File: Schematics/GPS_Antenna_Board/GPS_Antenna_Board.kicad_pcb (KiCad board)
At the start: 2 copper layers, 50 x 65 mm, 22 parts, among them J2 470804001, U1 SAM-M10Q, U2 LM66100DCKR

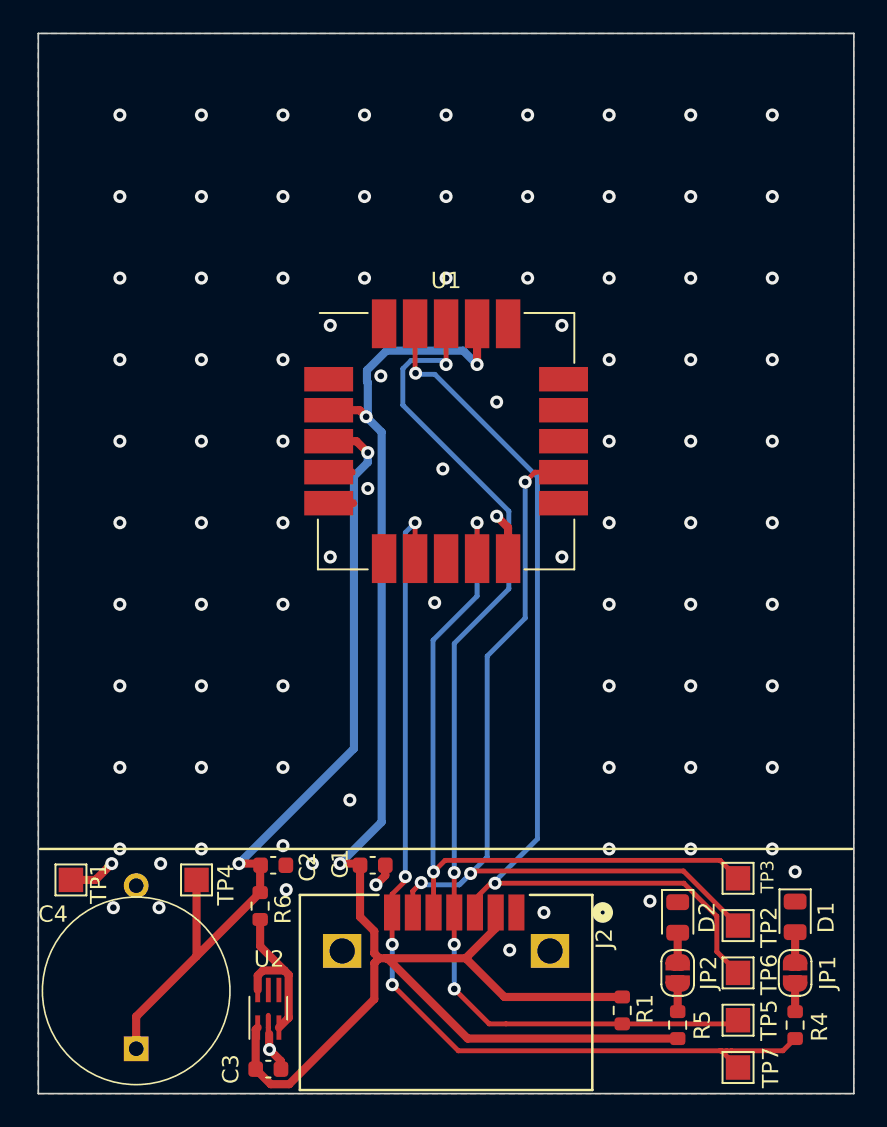
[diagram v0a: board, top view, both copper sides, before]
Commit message: Added mounting holes to GPS antenna board
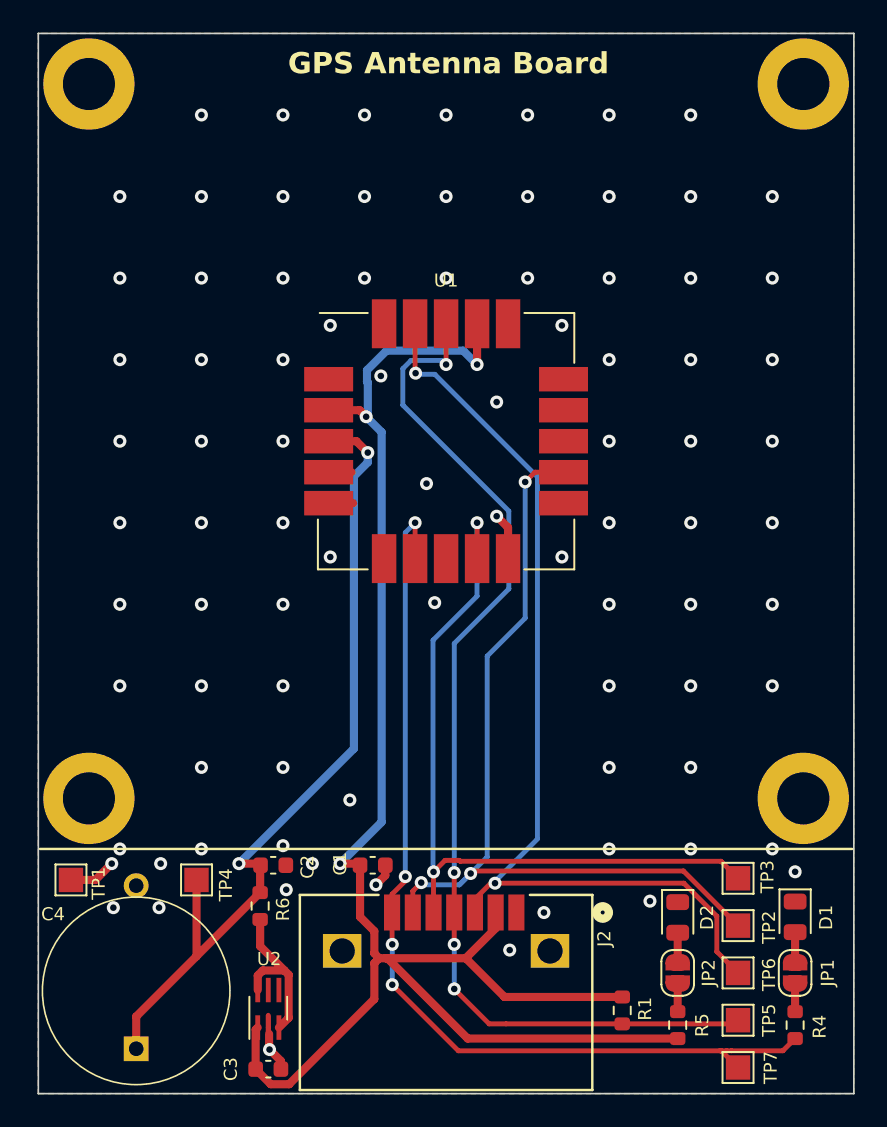
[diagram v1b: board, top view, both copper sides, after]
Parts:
- added H1: MountingHole, MountingHole:MountingHole_3.2mm_M3_DIN965_Pad, F.Cu at (125.8, 77.3)
- added H2: MountingHole, MountingHole:MountingHole_3.2mm_M3_DIN965_Pad, F.Cu at (169.6, 77.3)
- added H3: MountingHole, MountingHole:MountingHole_3.2mm_M3_DIN965_Pad, F.Cu at (125.8, 121.1)
- added H4: MountingHole, MountingHole:MountingHole_3.2mm_M3_DIN965_Pad, F.Cu at (169.6, 121.1)
- D1: value WHITE -> White
- D2: value GREEN -> Green
- TP1: value TP_PA0 -> TP_GND
- TP2: value TP_PA0 -> TP_SCL
- TP3: value TP_PA0 -> TP_SDA
- TP4: value TP_PA0 -> TP_BCKP
- TP5: value TP_PA0 -> TP_RST
- TP6: value TP_PA0 -> TP_INT
- TP7: value TP_PA0 -> TP_PPS
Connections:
- net EXTINT_GPS_D renamed GPS_EXTINT
- net GPS_3.3V renamed +3.3V
- net GPS_BCKP_BATT renamed BCKP_BATT
- net GPS_GND renamed GND
- net PPS_GPS_D renamed GPS_PPS
- net RST_GPS_D renamed GPS_RST
- net SCL_GPS_D renamed SCL
- net SDA_GPS_D renamed SDA
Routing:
- net GND: vias 92 -> 87
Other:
- board text added: "GPS Antenna Board"

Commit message: Verified part numbers & made ERC pass
Also cleaned up unnecessary footprints & added bulk filtering capacitor to GPS antenna board
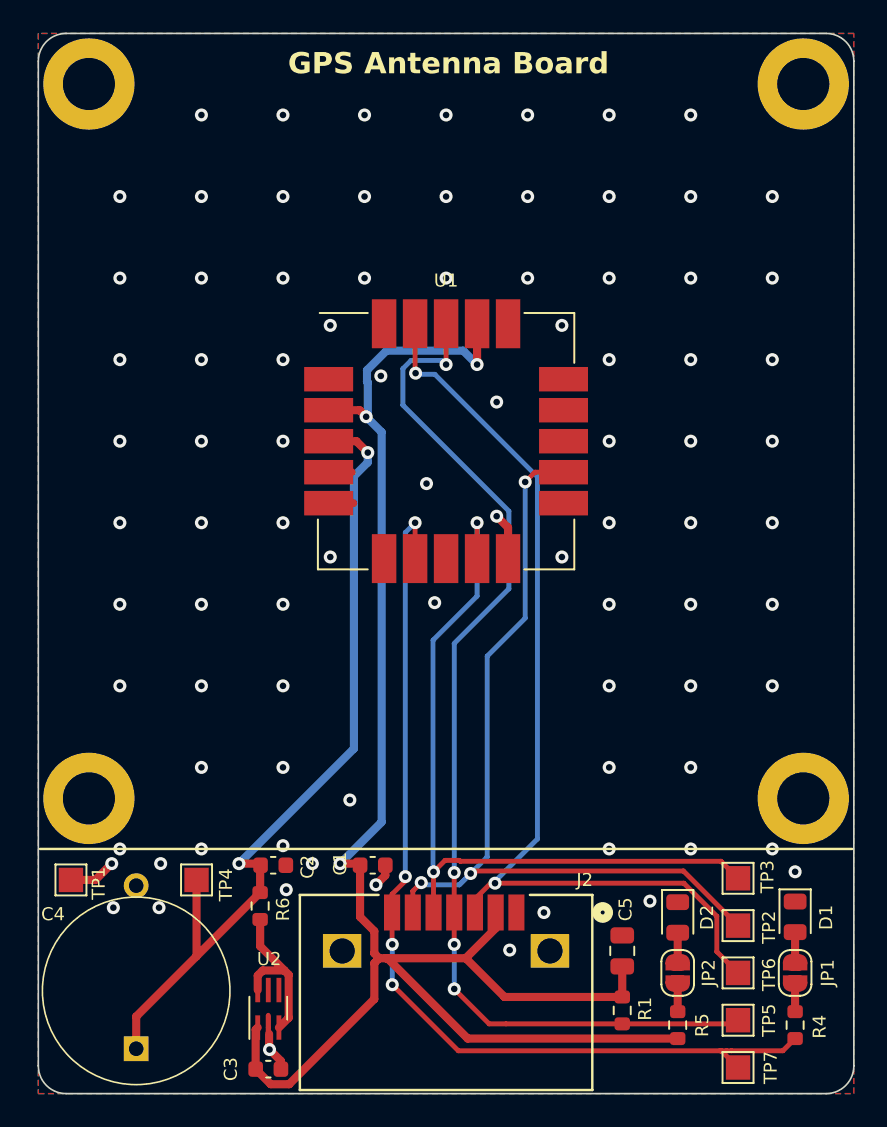
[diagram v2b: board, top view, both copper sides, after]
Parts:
- added C5: 47uF, Capacitor_SMD:C_0805_2012Metric, F.Cu at (158.5, 130.4)
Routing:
- net +3.3V: track 106.3 -> 108.2 mm
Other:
- outline, holes or cut-outs redrawn
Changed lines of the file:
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@@
     (property "ki_keywords" "470804001")
     (attr smd)
-    (fp_text reference "J2" (at 9.7 -3.3 90 unlocked) (layer "F.SilkS")
+    (fp_text reference "J2" (at 8.5 -6.9 unlocked) (layer "F.SilkS")
         (effects (font (size 0.8 0.8) (thickness 0.1)))
     )
@@
     )
   )
+  (footprint "Capacitor_SMD:C_0805_2012Metric" (layer "F.Cu")
+    (at 158.5 130.45 90)
+    (descr "Capacitor SMD 0805 (2012 Metric), square (rectangular) end terminal, IPC_7351 nominal, (Body size source: IPC-SM-782 page 76, https://www.pcb-3d.com/wordpress/wp-content/uploads/ipc-sm-782a_amendment_1_and_2.pdf, https://docs.google.com/spreadsheets/d/1BsfQQcO9C6DZCsRaXUlFlo91Tg2WpOkGARC1WS5S8t0/edit?usp=sharing), generated with kicad-footprint-generator")
+    (tags "capacitor")
+    (property "LCSC" "C16780")
+    (property "Sheetfile" "GPS_Antenna_Board.kicad_sch")
+    (property "Sheetname" "")
+    (property "ki_description" "Unpolarized capacitor")
+    (property "ki_keywords" "cap capacitor")
+    (attr smd)
+    (fp_text reference "C5" (at 2.55 0.2 90) (layer "F.SilkS")
+        (effects (font (size 0.8 0.8) (thickness 0.1)))
+    )
+    (fp_text value "47uF" (at 0 1.68 90) (layer "F.Fab")
+        (effects (font (size 1 1) (thickness 0.15)))
+    )
+    (fp_text user "${REFERENCE}" (at 0 0 90) (layer "F.Fab")
+        (effects (font (size 0.5 0.5) (thickness 0.08)))
+    )
+    (fp_line (start -0.261252 -0.735) (end 0.261252 -0.735)
+      (stroke (width 0.12) (type solid)) (layer "F.SilkS"))
+    (fp_line (start -0.261252 0.735) (end 0.261252 0.735)
+      (stroke (width 0.12) (type solid)) (layer "F.SilkS"))
+    (fp_line (start -1.7 -0.98) (end 1.7 -0.98)
+      (stroke (width 0.05) (type solid)) (layer "F.CrtYd"))
+    (fp_line (start -1.7 0.98) (end -1.7 -0.98)
+      (stroke (width 0.05) (type solid)) (layer "F.CrtYd"))
+    (fp_line (start 1.7 -0.98) (end 1.7 0.98)
+      (stroke (width 0.05) (type solid)) (layer "F.CrtYd"))
+    (fp_line (start 1.7 0.98) (end -1.7 0.98)
+      (stroke (width 0.05) (type solid)) (layer "F.CrtYd"))
+    (fp_line (start -1 -0.625) (end 1 -0.625)
+      (stroke (width 0.1) (type solid)) (layer "F.Fab"))
+    (fp_line (start -1 0.625) (end -1 -0.625)
+      (stroke (width 0.1) (type solid)) (layer "F.Fab"))
+    (fp_line (start 1 -0.625) (end 1 0.625)
+      (stroke (width 0.1) (type solid)) (layer "F.Fab"))
+    (fp_line (start 1 0.625) (end -1 0.625)
+      (stroke (width 0.1) (type solid)) (layer "F.Fab"))
+    (pad "1" smd roundrect (at -0.95 0 90) (size 1 1.45) (layers "F.Cu" "F.Paste" "F.Mask") (roundrect_rratio 0.25)
+      (net 2 "+3.3V") (pintype "passive"))
+    (pad "2" smd roundrect (at 0.95 0 90) (size 1 1.45) (layers "F.Cu" "F.Paste" "F.Mask") (roundrect_rratio 0.25)
+      (net 1 "GND") (pintype "passive"))
+    (model "${KICAD6_3DMODEL_DIR}/Capacitor_SMD.3dshapes/C_0805_2012Metric.wrl"
+      (offset (xyz 0 0 0))
+      (scale (xyz 1 1 1))
+      (rotate (xyz 0 0 0))
+    )
+  )
   (footprint "Jumper:SolderJumper-2_P1.3mm_Open_RoundedPad1.0x1.5mm" (layer "F.Cu")
     (at 169.1 131.8 -90)
@@
   (gr_line (start 169.6 121.1) (end 169.600002 124.2)
     (stroke (width 0.2) (type default)) (layer "Dwgs.User"))
-  (gr_rect (start 206.7 78) (end 256.7 128)
-    (stroke (width 0.2) (type default)) (fill none) (layer "Dwgs.User"))
   (gr_line (start 125.800002 124.2) (end 125.8 121.1)
     (stroke (width 0.2) (type solid)) (layer "Dwgs.User"))
-  (gr_rect (start 211.7 83) (end 251.7 123)
-    (stroke (width 0.2) (type default)) (fill none) (layer "Dwgs.User"))
   (gr_line (start 172.7 121.099998) (end 169.6 121.1)
     (stroke (width 0.2) (type solid)) (layer "Dwgs.User"))
@@
   (gr_line (start 125.8 121.1) (end 122.7 121.100002)
     (stroke (width 0.2) (type default)) (layer "Dwgs.User"))
-  (gr_line (start 122.7 74.2) (end 172.7 74.2)
-    (stroke (width 0.1) (type default)) (layer "Edge.Cuts"))
-  (gr_line (start 172.7 74.2) (end 172.7 139.2)
-    (stroke (width 0.1) (type default)) (layer "Edge.Cuts"))
-  (gr_line (start 122.7 139.2) (end 122.7 74.2)
-    (stroke (width 0.1) (type default)) (layer "Edge.Cuts"))
-  (gr_line (start 172.7 139.2) (end 122.7 139.2)
+  (gr_line (start 124.4 74.2) (end 171 74.2)
+    (stroke (width 0.1) (type default)) (layer "Edge.Cuts"))
+  (gr_line (start 172.7 75.9) (end 172.7 137.5)
+    (stroke (width 0.1) (type default)) (layer "Edge.Cuts"))
+  (gr_arc (start 124.4 139.2) (mid 123.197918 138.702082) (end 122.7 137.5)
+    (stroke (width 0.1) (type default)) (layer "Edge.Cuts"))
+  (gr_arc (start 172.7 137.5) (mid 172.202082 138.702083) (end 171 139.2)
+    (stroke (width 0.1) (type default)) (layer "Edge.Cuts"))
+  (gr_line (start 122.7 137.5) (end 122.7 75.9)
+    (stroke (width 0.1) (type default)) (layer "Edge.Cuts"))
+  (gr_line (start 171 139.2) (end 124.4 139.2)
+    (stroke (width 0.1) (type default)) (layer "Edge.Cuts"))
+  (gr_arc (start 122.7 75.9) (mid 123.197918 74.697917) (end 124.4 74.2)
+    (stroke (width 0.1) (type default)) (layer "Edge.Cuts"))
+  (gr_arc (start 171 74.2) (mid 172.202082 74.697918) (end 172.7 75.9)
     (stroke (width 0.1) (type default)) (layer "Edge.Cuts"))
   (gr_text "GPS Antenna Board" (at 138 76.8) (layer "F.SilkS" knockout)
@@
   (segment (start 144.1 130.9) (end 144 130.9) (width 0.5) (layer "F.Cu") (net 2))
   (segment (start 150.739999 128.095301) (end 150.739999 129.061897) (width 0.5) (layer "F.Cu") (net 2))
+  (segment (start 158.5 133.275) (end 158.5 131.4) (width 0.5) (layer "F.Cu") (net 2))
   (segment (start 141.2 125.1) (end 142.425 125.1) (width 0.5) (layer "F.Cu") (net 2))
   (segment (start 136.95 138.625) (end 138.079594 138.625) (width 0.5) (layer "F.Cu") (net 2))

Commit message: Add silkscreen & final PCB adjustments
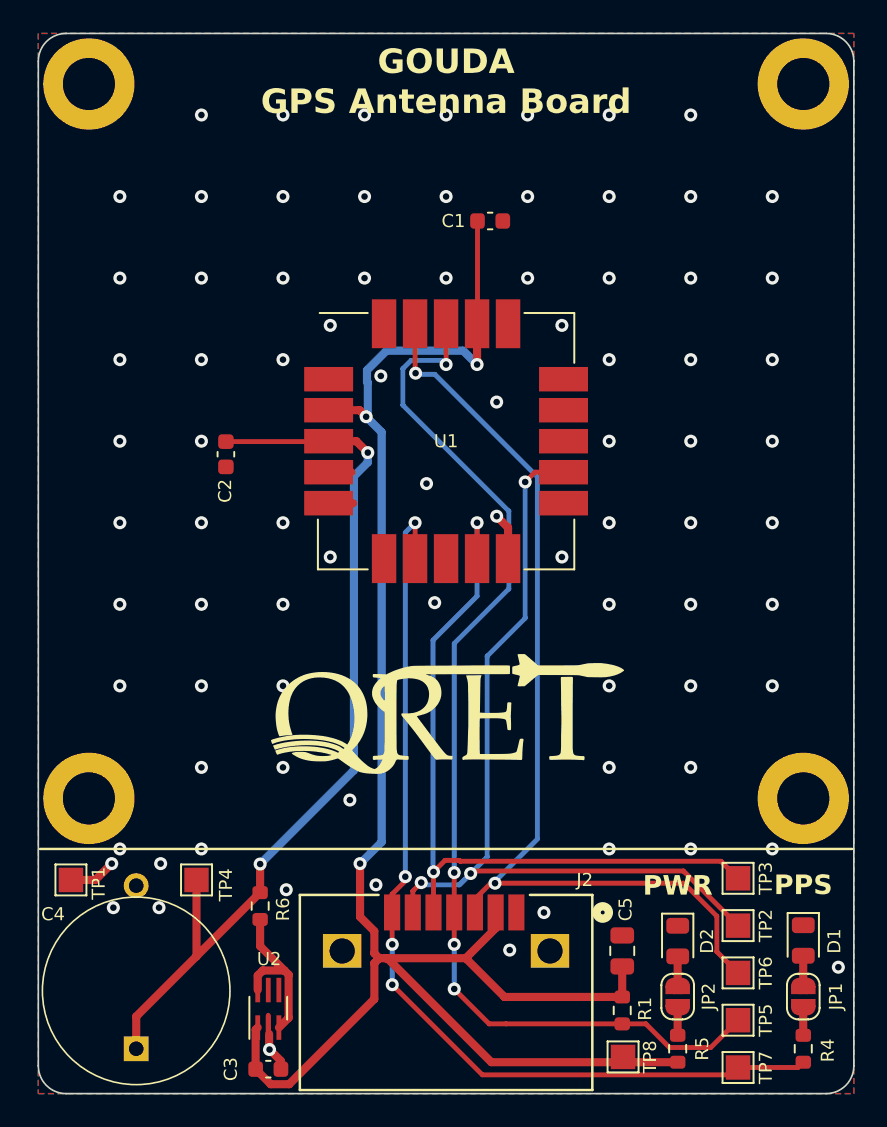
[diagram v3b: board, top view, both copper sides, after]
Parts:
- added TP8: TP_3.3V, TestPoint:TestPoint_Pad_1.5x1.5mm, F.Cu at (158.6, 136.9)
- moved C1 40.2 mm to (150.4, 85.7)
- moved C2 25.4 mm to (134.2, 100.0), turned to 90 degrees
- moved D1 1.53 mm to (169.6, 129.8)
- moved JP1 1.53 mm to (169.6, 133.2)
- moved R4 1.53 mm to (169.6, 136.4)
- moved D2 1.45 mm to (161.9, 129.8)
- moved JP2 1.45 mm to (161.9, 133.2)
- moved R5 1.45 mm to (161.9, 136.4)
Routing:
- net +3.3V: track 108.2 -> 113.3 mm
- net BCKP_BATT: track 51.9 -> 56.3 mm
- net GND: track 13.8 -> 12.3 mm, vias 87 -> 83
- net GPS_RST: track 66.0 -> 67.2 mm
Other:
- board text added: "GOUDA"
- board text added: "Gouda Rev 1.0 QRET Mar 2024 Tristan Alderson Kennan Bays"
- board text added: "PPS"
- board text added: "PWR"

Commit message: Updated Debug/PPS/Power LED resistors
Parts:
- J2: value 470804001 -> SATA Conn. (Male)
- R5: value 2.2k -> 1.8k
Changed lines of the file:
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@@
         (effects (font (size 0.8 0.8) (thickness 0.1)))
     )
-    (fp_text value "470804001" (at 0 -4.904699 unlocked) (layer "F.Fab")
+    (fp_text value "SATA Conn. (Male)" (at 0 -4.904699 unlocked) (layer "F.Fab")
         (effects (font (size 1 1) (thickness 0.15)))
     )
@@
       (stroke (width 0.508) (type solid)) (fill none) (layer "F.Fab"))
     (pad "1" smd rect (at 4.309999 -4.904699) (size 0.9906 2.2098) (layers "F.Cu" "F.Paste" "F.Mask")
-      (net 1 "GND") (pinfunction "1") (pintype "unspecified"))
+      (net 1 "GND") (pinfunction "1") (pintype "passive"))
     (pad "2" smd rect (at 3.039999 -4.904699) (size 0.9906 2.2098) (layers "F.Cu" "F.Paste" "F.Mask")
-      (net 2 "+3.3V") (pinfunction "2") (pintype "unspecified"))
+      (net 2 "+3.3V") (pinfunction "2") (pintype "passive"))
     (pad "3" smd rect (at 1.769999 -4.904699) (size 0.9906 2.2098) (layers "F.Cu" "F.Paste" "F.Mask")
-      (net 6 "GPS_EXTINT") (pinfunction "3") (pintype "unspecified"))
+      (net 6 "GPS_EXTINT") (pinfunction "3") (pintype "passive"))
     (pad "4" smd rect (at 0.499999 -4.904699) (size 0.9906 2.2098) (layers "F.Cu" "F.Paste" "F.Mask")
-      (net 7 "GPS_RST") (pinfunction "4") (pintype "unspecified"))
+      (net 7 "GPS_RST") (pinfunction "4") (pintype "passive"))
     (pad "5" smd rect (at -0.770001 -4.904699) (size 0.9906 2.2098) (layers "F.Cu" "F.Paste" "F.Mask")
-      (net 8 "SDA") (pinfunction "5") (pintype "unspecified"))
+      (net 8 "SDA") (pinfunction "5") (pintype "passive"))
     (pad "6" smd rect (at -2.040001 -4.904699) (size 0.9906 2.2098) (layers "F.Cu" "F.Paste" "F.Mask")
-      (net 9 "SCL") (pinfunction "6") (pintype "unspecified"))
+      (net 9 "SCL") (pinfunction "6") (pintype "passive"))
     (pad "7" smd rect (at -3.310001 -4.904699) (size 0.9906 2.2098) (layers "F.Cu" "F.Paste" "F.Mask")
-      (net 10 "GPS_PPS") (pinfunction "7") (pintype "unspecified"))
+      (net 10 "GPS_PPS") (pinfunction "7") (pintype "passive"))
     (pad "8" thru_hole rect (at -6.37 -2.544785 90) (size 2.0574 2.3622) (drill 1.5494) (layers "*.Cu" "*.Mask"))
     (pad "9" thru_hole rect (at 6.37 -2.544785 90) (size 2.0574 2.3622) (drill 1.5494) (layers "*.Cu" "*.Mask"))
@@
     (descr "Resistor SMD 0603 (1608 Metric), square (rectangular) end terminal, IPC_7351 nominal, (Body size source: IPC-SM-782 page 72, https://www.pcb-3d.com/wordpress/wp-content/uploads/ipc-sm-782a_amendment_1_and_2.pdf), generated with kicad-footprint-generator")
     (tags "resistor")
-    (property "LCSC" "C4190")
+    (property "LCSC" "C4177")
     (property "Sheetfile" "GPS_Antenna_Board.kicad_sch")
     (property "Sheetname" "")
@@
         (effects (font (size 0.8 0.8) (thickness 0.1)))
     )
-    (fp_text value "2.2k" (at 0 1.43 90) (layer "F.Fab")
-        (effects (font (size 1 1) (thickness 0.15)))
-    )
+    (fp_text value "1.8k" (at 0 1.43 90) (layer "F.Fab")
+        (effects (font (size 1 1) (thickness 0.15)))
+    )
